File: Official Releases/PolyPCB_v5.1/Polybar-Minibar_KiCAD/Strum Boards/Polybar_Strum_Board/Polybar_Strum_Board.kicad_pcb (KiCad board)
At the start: 2 copper layers, 185 x 38 mm, 25 parts, among them U1 ProMicro

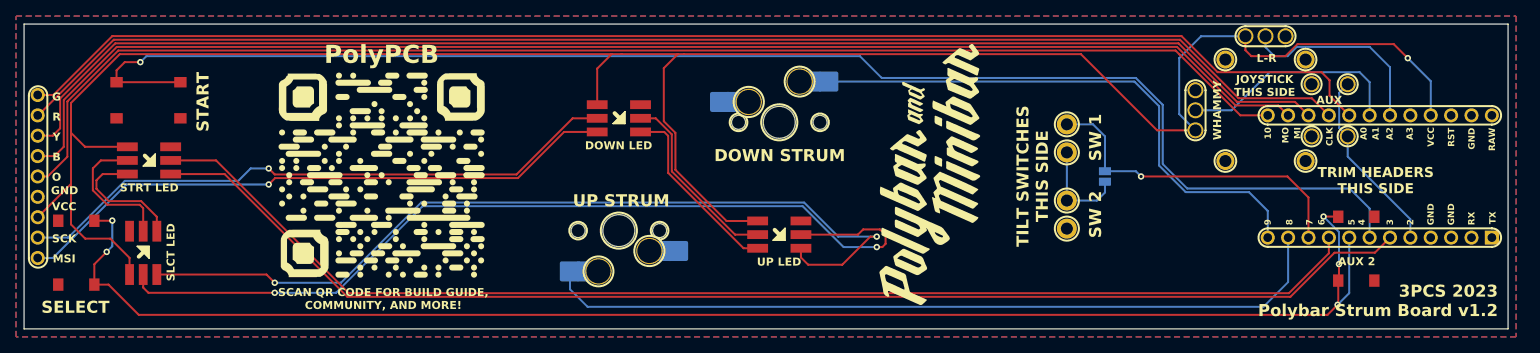
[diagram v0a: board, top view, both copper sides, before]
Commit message: Linked everything in the PCB to the schematic
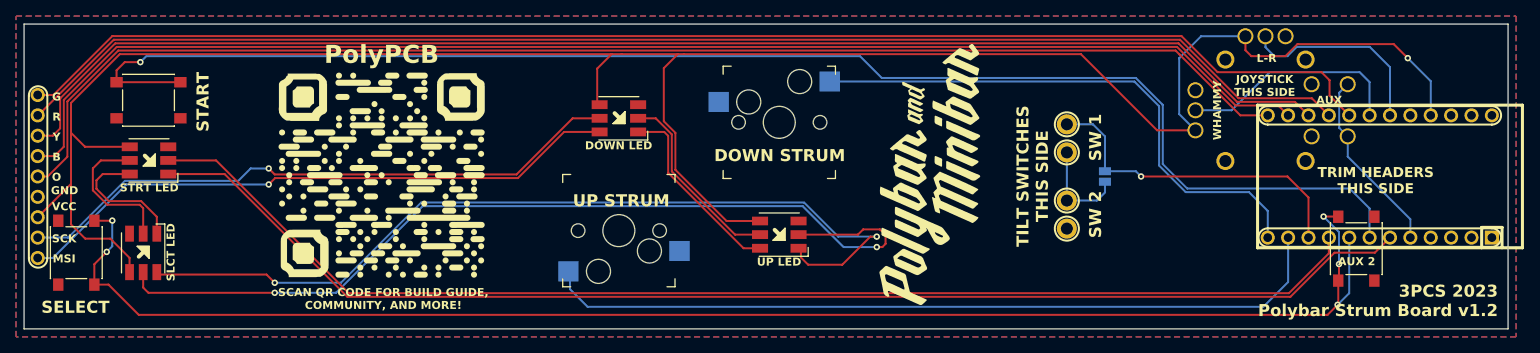
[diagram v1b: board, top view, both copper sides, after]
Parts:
- D1, D2, D3, D4: renamed from D5; footprint Controller_Inputs:LED_RGB_5050_DOTSTAR -> LED_SMD:LED_RGB_5050-6
- SJ1: renamed from SINGLE TILT JUMPER; value SolderJumper-2_P1.3mm_Open_Pad1.0x1.5mm -> Conn_01x02_Pin; footprint Jumper:SolderJumper-2_P1.3mm_Open_Pad1.0x1.5mm -> Polybar:Solder_Jumper
- SW1, SW2, SW3: renamed from REF**; value SW_SPST_PTS645 -> MX_SW_solder
- SW4, SW5: renamed from  ; footprint marbastlib-mx:SW_MX_HS_1u -> Polybar:Kailh_Hotswap_MX; moved to F.Cu
- TP1, TP17, TP2, TP3: renamed from ?; value (none) -> TestPoint; footprint (none) -> Polybar:test_point_2
- TP10, TP11, TP12, TP14, TP15, TP16, TP4, TP6, TP8: renamed from ?; value (none) -> TestPoint; footprint (none) -> Polybar:test_point
- U1: footprint Controller_Inputs:KB2040-ProMicroPins -> Polybar:KB2040-ProMicroPins
- U2: renamed from U**; footprint Controller_Inputs:RKJXV1224005 -> Polybar:RKJXV1224005
- turned SW4 to 0 degrees
- turned SW5 to 180 degrees
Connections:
- net Net-(D1-C0) renamed 3_sck
- net Net-(D1-D0) renamed 3_mosi
- net Net-(D2-C0) renamed 2_sck
- net Net-(D2-D0) renamed 2_mosi
- net Net-(D3-C0) renamed 1_sck
- net Net-(D3-D0) renamed 1_mosi
- D1 pad 5: Net-(D4-C0) -> fret_sck
- D1 pad 6: Net-(D4-D0) -> fret_mosi
- SJ1 pad 2: Tilt -> Tilt_2
- SW1 pad 1: GND -> Select
- SW1 pad 2: Select -> GND
- SW3 pad 1: Start -> GND
- SW3 pad 2: GND -> Start
- SW4 pad : GND -> (no net)
- SW4 pad 2: Down -> GND
- SW5 pad : GND -> (no net)
- SW5 pad 1: GND -> Up
- U1 pad 1: (no net) -> unconnected-(U1-TX0/PD3-Pad1)
- U1 pad 2: (no net) -> unconnected-(U1-RX1/PD2-Pad2)
- U1 pad 20: (no net) -> unconnected-(U1-A3/PF4-Pad20)
- U1 pad 22: (no net) -> unconnected-(U1-RST-Pad22)
- U1 pad 24: (no net) -> unconnected-(U1-RAW-Pad24)
- U2 pad SH: SW -> (no net)
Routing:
- net fret_sck: track 0.00 -> 76.5 mm, vias 0 -> 1
- net Net-(D4-C0): track 76.5 -> 0.00 mm, vias 1 -> 0
- net fret_mosi: track 0.00 -> 76.3 mm, vias 0 -> 1
- net Net-(D4-D0): track 76.3 -> 0.00 mm, vias 1 -> 0
- net Tilt: track 54.0 -> 41.4 mm
- net Tilt_2: track 0.00 -> 12.5 mm
